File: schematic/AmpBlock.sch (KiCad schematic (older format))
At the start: 12 parts, among them IC8 LTC6090CS8E#PBF

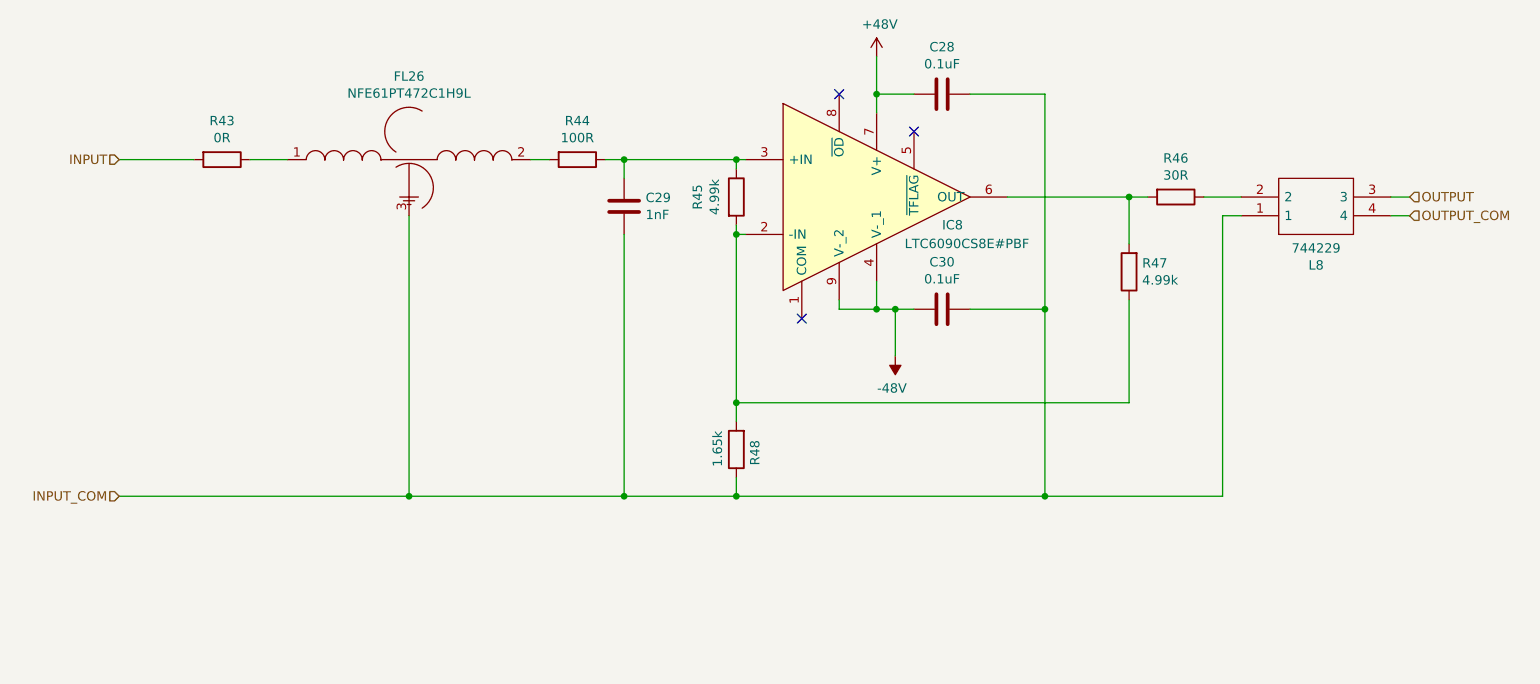
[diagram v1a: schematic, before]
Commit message: Board updates and starting to add more capacitors
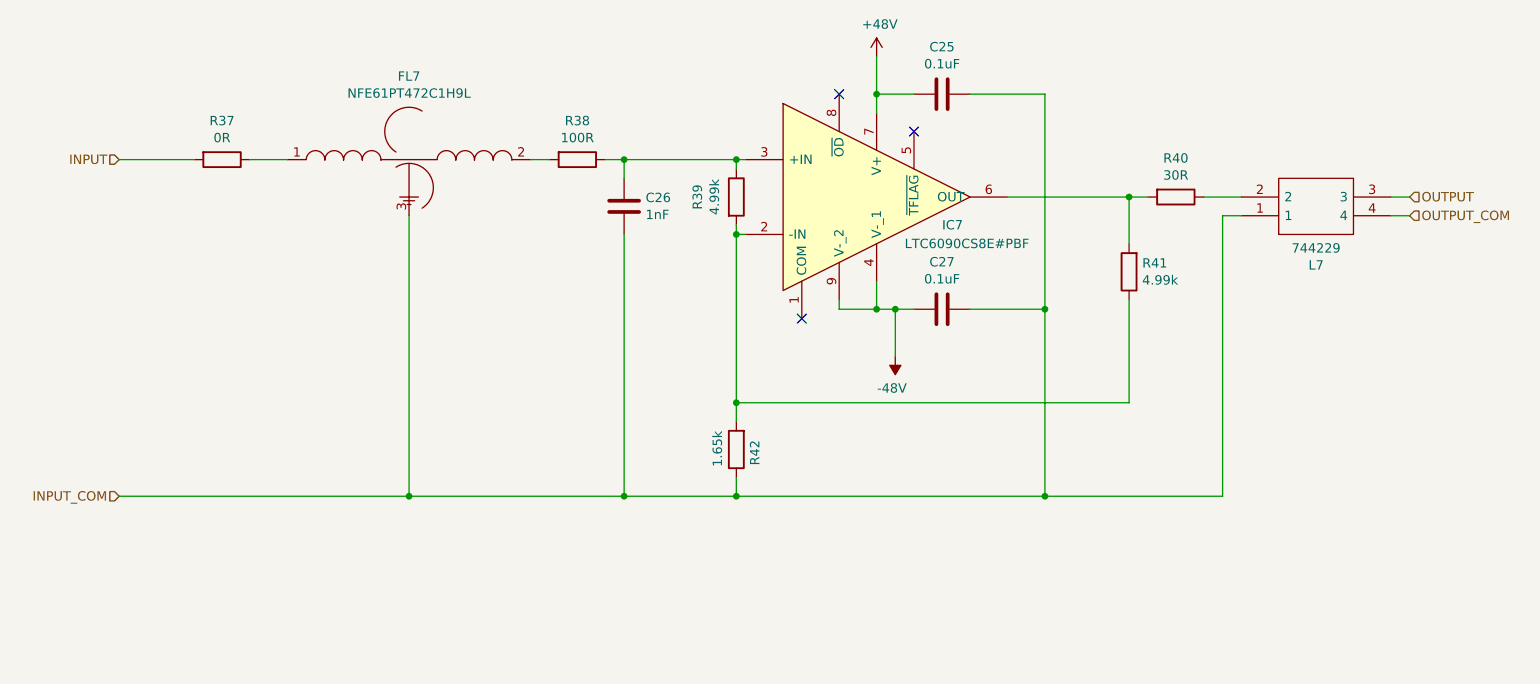
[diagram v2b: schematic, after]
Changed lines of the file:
@@
 $Descr A4 11693 8268
 encoding utf-8
-Sheet 26 33
+Sheet 8 33
 Title "Amplifier block"
 Date ""
@@
 AR Path="/5CAE2EB0/5C968DBB" Ref="R188"  Part="1"
 AR Path="/5C968DBB" Ref="R?"  Part="1"
-F 0 "R?" V 3743 3400 50  0000 C CNN
+F 0 "R38" V 3743 3400 50  0000 C CNN
 F 1 "100R" V 3834 3400 50  0000 C CNN
 F 2 "Resistor_SMD:R_0603_1608Metric" V 3880 3400 50  0001 C CNN
@@
 AR Path="/5CAE2EB0/5C969C02" Ref="R192"  Part="1"
 AR Path="/5C969C02" Ref="R?"  Part="1"
-F 0 "R?" V 4700 4900 50  0000 L CNN
+F 0 "R42" V 4700 4900 50  0000 L CNN
 F 1 "1.65k" V 4900 4850 50  0000 L CNN
 F 2 "Resistor_SMD:R_0603_1608Metric" V 4730 4950 50  0001 C CNN
@@
 AR Path="/5CAE2EB0/5C96A29C" Ref="R191"  Part="1"
 AR Path="/5C96A29C" Ref="R?"  Part="1"
-F 0 "R?" H 6830 3954 50  0000 R CNN
+F 0 "R41" H 6830 3954 50  0000 R CNN
 F 1 "4.99k" H 6830 4045 50  0000 R CNN
 F 2 "Resistor_SMD:R_0603_1608Metric" V 6830 4000 50  0001 C CNN
@@
 AR Path="/5CAE2EB0/5C96A628" Ref="C101"  Part="1"
 AR Path="/5C96A628" Ref="C?"  Part="1"
-F 0 "C?" H 4315 3696 50  0000 L CNN
+F 0 "C26" H 4315 3696 50  0000 L CNN
 F 1 "1nF" H 4315 3605 50  0000 L CNN
 F 2 "Capacitor_SMD:C_0603_1608Metric" H 4238 3500 50  0001 C CNN
@@
 AR Path="/5CAE2EB0/5C96EFD0" Ref="#PWR073"  Part="1"
 AR Path="/5C96EFD0" Ref="#PWR?"  Part="1"
-F 0 "#PWR063" H 5550 2700 50  0001 C CNN
+F 0 "#PWR023" H 5550 2700 50  0001 C CNN
 F 1 "+48V" H 5567 3023 50  0000 C CNN
 F 2 "" H 5550 2850 50  0001 C CNN
@@
 AR Path="/5CAE2EB0/5C96F7F1" Ref="#PWR074"  Part="1"
 AR Path="/5C96F7F1" Ref="#PWR?"  Part="1"
-F 0 "#PWR064" H 5650 4300 50  0001 C CNN
+F 0 "#PWR024" H 5650 4300 50  0001 C CNN
 F 1 "-48V" H 5668 4623 50  0000 C CNN
 F 2 "" H 5650 4450 50  0001 C CNN
@@
 AR Path="/5CAE2EB0/5C96FD85" Ref="C100"  Part="1"
 AR Path="/5C96FD85" Ref="C?"  Part="1"
-F 0 "C?" V 5648 3050 50  0000 C CNN
+F 0 "C25" V 5648 3050 50  0000 C CNN
 F 1 "0.1uF" V 5739 3050 50  0000 C CNN
 F 2 "Capacitor_SMD:C_0603_1608Metric" H 5938 2900 50  0001 C CNN
@@
 AR Path="/5CAE2EB0/5C97026D" Ref="C102"  Part="1"
 AR Path="/5C97026D" Ref="C?"  Part="1"
-F 0 "C?" V 5648 4200 50  0000 C CNN
+F 0 "C27" V 5648 4200 50  0000 C CNN
 F 1 "0.1uF" V 5739 4200 50  0000 C CNN
 F 2 "Capacitor_SMD:C_0603_1608Metric" H 5938 4050 50  0001 C CNN
@@
 AR Path="/5CAE2E6A/5E7F6ABF" Ref="FL31"  Part="1"
 AR Path="/5CAE2EB0/5E7F6ABF" Ref="FL32"  Part="1"
-F 0 "FL?" H 3050 3845 50  0000 C CNN
+F 0 "FL7" H 3050 3845 50  0000 C CNN
 F 1 "NFE61PT472C1H9L" H 3050 3754 50  0000 C CNN
 F 2 "ARTIQAmp:NFE61" H 3400 3650 50  0001 L CNN
@@
 AR Path="/5CAE2EB0/5F650121" Ref="R187"  Part="1"
 AR Path="/5F650121" Ref="R?"  Part="1"
-F 0 "R?" V 1843 3400 50  0000 C CNN
+F 0 "R37" V 1843 3400 50  0000 C CNN
 F 1 "0R" V 1934 3400 50  0000 C CNN
 F 2 "Resistor_SMD:R_0603_1608Metric" V 1980 3400 50  0001 C CNN
@@
 AR Path="/5CAE2EB0/5F6588CE" Ref="R189"  Part="1"
 AR Path="/5F6588CE" Ref="R?"  Part="1"
-F 0 "R?" V 4593 3600 50  0000 C CNN
+F 0 "R39" V 4593 3600 50  0000 C CNN
 F 1 "4.99k" V 4684 3600 50  0000 C CNN
 F 2 "Resistor_SMD:R_0603_1608Metric" V 4730 3600 50  0001 C CNN
@@
 AR Path="/5CAE2EB0/5F678EAA" Ref="R190"  Part="1"
 AR Path="/5F678EAA" Ref="R?"  Part="1"
-F 0 "R?" V 6943 3600 50  0000 C CNN
+F 0 "R40" V 6943 3600 50  0000 C CNN
 F 1 "30R" V 7034 3600 50  0000 C CNN
 F 2 "Resistor_SMD:R_0603_1608Metric" V 7080 3600 50  0001 C CNN
@@
 AR Path="/5CAE2E6A/5F68D18B" Ref="L31"  Part="1"
 AR Path="/5CAE2EB0/5F68D18B" Ref="L32"  Part="1"
-F 0 "L?" H 7900 3965 50  0000 C CNN
+F 0 "L7" H 7900 3965 50  0000 C CNN
 F 1 "744229" H 7900 3874 50  0000 C CNN
 F 2 "ARTIQAmp:WE-SL2" H 8150 3800 50  0001 L CNN
@@
 AR Path="/5CAE2E6A/5F68D7CC" Ref="IC31"  Part="1"
 AR Path="/5CAE2EB0/5F68D7CC" Ref="IC32"  Part="1"
-F 0 "IC?" H 5900 3450 50  0000 L CNN
+F 0 "IC7" H 5900 3450 50  0000 L CNN
 F 1 "LTC6090CS8E#PBF" H 5700 3350 50  0000 L CNN
 F 2 "ARTIQAmp:SOIC127P599X175-9N" H 5600 4200 50  0001 L CNN

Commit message: Many updates to layout; nearing final design
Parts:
- added R207, R208: 0R, Resistor_SMD:R_0603_1608Metric, symbol Device:R
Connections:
- net INPUT_COM: now also R207.2, R208.2
- new net GND: R207.1, R208.1
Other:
- note added: "Optional connections to ground plane"

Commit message: Penultimate tweaks
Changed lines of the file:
@@
 AR Path="/5CAE2EB0/5FE9E532" Ref="R188"  Part="1"
 AR Path="/5FE9E532" Ref="R?"  Part="1"
-F 0 "R38" V 3743 3400 50  0000 C CNN
+F 0 "R158" V 3743 3400 50  0000 C CNN
 F 1 "100R" V 3834 3400 50  0000 C CNN
 F 2 "Resistor_SMD:R_0603_1608Metric" V 3880 3400 50  0001 C CNN
@@
 AR Path="/5CAE2EB0/5C969C02" Ref="R192"  Part="1"
 AR Path="/5C969C02" Ref="R?"  Part="1"
-F 0 "R42" V 4700 4900 50  0000 L CNN
+F 0 "R162" V 4700 4900 50  0000 L CNN
 F 1 "1.65k" V 4900 4850 50  0000 L CNN
 F 2 "Resistor_SMD:R_0603_1608Metric" V 4730 4950 50  0001 C CNN
@@
 AR Path="/5CAE2EB0/5C96A29C" Ref="R191"  Part="1"
 AR Path="/5C96A29C" Ref="R?"  Part="1"
-F 0 "R41" H 6830 3954 50  0000 R CNN
+F 0 "R161" H 6830 3954 50  0000 R CNN
 F 1 "4.99k" H 6830 4045 50  0000 R CNN
 F 2 "Resistor_SMD:R_0603_1608Metric" V 6830 4000 50  0001 C CNN
@@
 AR Path="/5CAE2EB0/5C96A628" Ref="C101"  Part="1"
 AR Path="/5C96A628" Ref="C?"  Part="1"
-F 0 "C26" H 4315 3696 50  0000 L CNN
+F 0 "C86" H 4315 3696 50  0000 L CNN
 F 1 "1nF" H 4315 3605 50  0000 L CNN
 F 2 "Capacitor_SMD:C_0603_1608Metric" H 4238 3500 50  0001 C CNN
@@
 AR Path="/5CAE2EB0/5C96EFD0" Ref="#PWR073"  Part="1"
 AR Path="/5C96EFD0" Ref="#PWR?"  Part="1"
-F 0 "#PWR023" H 5550 2700 50  0001 C CNN
+F 0 "#PWR063" H 5550 2700 50  0001 C CNN
 F 1 "+48V" H 5567 3023 50  0000 C CNN
 F 2 "" H 5550 2850 50  0001 C CNN
@@
 AR Path="/5CAE2EB0/5FE9E537" Ref="#PWR074"  Part="1"
 AR Path="/5FE9E537" Ref="#PWR?"  Part="1"
-F 0 "#PWR024" H 5650 4300 50  0001 C CNN
+F 0 "#PWR064" H 5650 4300 50  0001 C CNN
 F 1 "-48V" H 5668 4623 50  0000 C CNN
 F 2 "" H 5650 4450 50  0001 C CNN
@@
 AR Path="/5CAE2EB0/5C96FD85" Ref="C100"  Part="1"
 AR Path="/5C96FD85" Ref="C?"  Part="1"
-F 0 "C25" V 5648 3050 50  0000 C CNN
+F 0 "C85" V 5648 3050 50  0000 C CNN
 F 1 "0.1uF" V 5739 3050 50  0000 C CNN
 F 2 "Capacitor_SMD:C_0603_1608Metric" H 5938 2900 50  0001 C CNN
@@
 AR Path="/5CAE2EB0/5FE9E539" Ref="C102"  Part="1"
 AR Path="/5FE9E539" Ref="C?"  Part="1"
-F 0 "C27" V 5648 4200 50  0000 C CNN
+F 0 "C87" V 5648 4200 50  0000 C CNN
 F 1 "0.1uF" V 5739 4200 50  0000 C CNN
 F 2 "Capacitor_SMD:C_0603_1608Metric" H 5938 4050 50  0001 C CNN
@@
 AR Path="/5CAE2E6A/5E7F6ABF" Ref="FL31"  Part="1"
 AR Path="/5CAE2EB0/5E7F6ABF" Ref="FL32"  Part="1"
-F 0 "FL7" H 3050 3845 50  0000 C CNN
+F 0 "FL27" H 3050 3845 50  0000 C CNN
 F 1 "NFE61PT472C1H9L" H 3050 3754 50  0000 C CNN
 F 2 "ARTIQAmp:NFE61" H 3400 3650 50  0001 L CNN
@@
 AR Path="/5CAE2EB0/5F650121" Ref="R187"  Part="1"
 AR Path="/5F650121" Ref="R?"  Part="1"
-F 0 "R37" V 1843 3400 50  0000 C CNN
+F 0 "R157" V 1843 3400 50  0000 C CNN
 F 1 "0R" V 1934 3400 50  0000 C CNN
 F 2 "Resistor_SMD:R_0603_1608Metric" V 1980 3400 50  0001 C CNN
@@
 AR Path="/5CAE2EB0/5F6588CE" Ref="R189"  Part="1"
 AR Path="/5F6588CE" Ref="R?"  Part="1"
-F 0 "R39" V 4593 3600 50  0000 C CNN
+F 0 "R159" V 4593 3600 50  0000 C CNN
 F 1 "4.99k" V 4684 3600 50  0000 C CNN
 F 2 "Resistor_SMD:R_0603_1608Metric" V 4730 3600 50  0001 C CNN
@@
 AR Path="/5CAE2EB0/5F678EAA" Ref="R190"  Part="1"
 AR Path="/5F678EAA" Ref="R?"  Part="1"
-F 0 "R40" V 6943 3600 50  0000 C CNN
+F 0 "R160" V 6943 3600 50  0000 C CNN
 F 1 "30R" V 7034 3600 50  0000 C CNN
 F 2 "Resistor_SMD:R_0603_1608Metric" V 7080 3600 50  0001 C CNN
@@
 AR Path="/5CAE2E6A/5F68D18B" Ref="L31"  Part="1"
 AR Path="/5CAE2EB0/5F68D18B" Ref="L32"  Part="1"
-F 0 "L7" H 7900 3965 50  0000 C CNN
+F 0 "L27" H 7900 3965 50  0000 C CNN
 F 1 "744229" H 7900 3874 50  0000 C CNN
 F 2 "ARTIQAmp:WE-SL2" H 8150 3800 50  0001 L CNN
@@
 AR Path="/5CAE2E6A/5F68D7CC" Ref="IC31"  Part="1"
 AR Path="/5CAE2EB0/5F68D7CC" Ref="IC32"  Part="1"
-F 0 "IC7" H 5900 3450 50  0000 L CNN
+F 0 "IC27" H 5900 3450 50  0000 L CNN
 F 1 "LTC6090CS8E#PBF" H 5700 3350 50  0000 L CNN
 F 2 "ARTIQAmp:SOIC127P599X175-9N" H 5600 4200 50  0001 L CNN
@@
 AR Path="/5CAE2EB0/5F8DFD1E" Ref="#PWR0135"  Part="1"
 AR Path="/5CAE2E52/5F8DFD1E" Ref="#PWR0136"  Part="1"
-F 0 "#PWR0111" H 3050 5650 50  0001 C CNN
+F 0 "#PWR0136" H 3050 5650 50  0001 C CNN
 F 1 "GND" H 3055 5727 50  0000 C CNN
 F 2 "" H 3050 5900 50  0001 C CNN
@@
 AR Path="/5CAE2EB0/5F8E08A0" Ref="R253"  Part="1"
 AR Path="/5F8E08A0" Ref="R?"  Part="1"
-F 0 "R205" V 2800 5500 50  0000 L CNN
+F 0 "R255" V 2800 5500 50  0000 L CNN
 F 1 "0R" V 3000 5450 50  0000 L CNN
 F 2 "Resistor_SMD:R_0603_1608Metric" V 2830 5550 50  0001 C CNN
@@
 AR Path="/5CAE2EB0/5F8E1BE6" Ref="R254"  Part="1"
 AR Path="/5F8E1BE6" Ref="R?"  Part="1"
-F 0 "R206" V 3100 5500 50  0000 L CNN
+F 0 "R256" V 3100 5500 50  0000 L CNN
 F 1 "0R" V 3300 5450 50  0000 L CNN
 F 2 "Resistor_SMD:R_0603_1608Metric" V 3130 5550 50  0001 C CNN

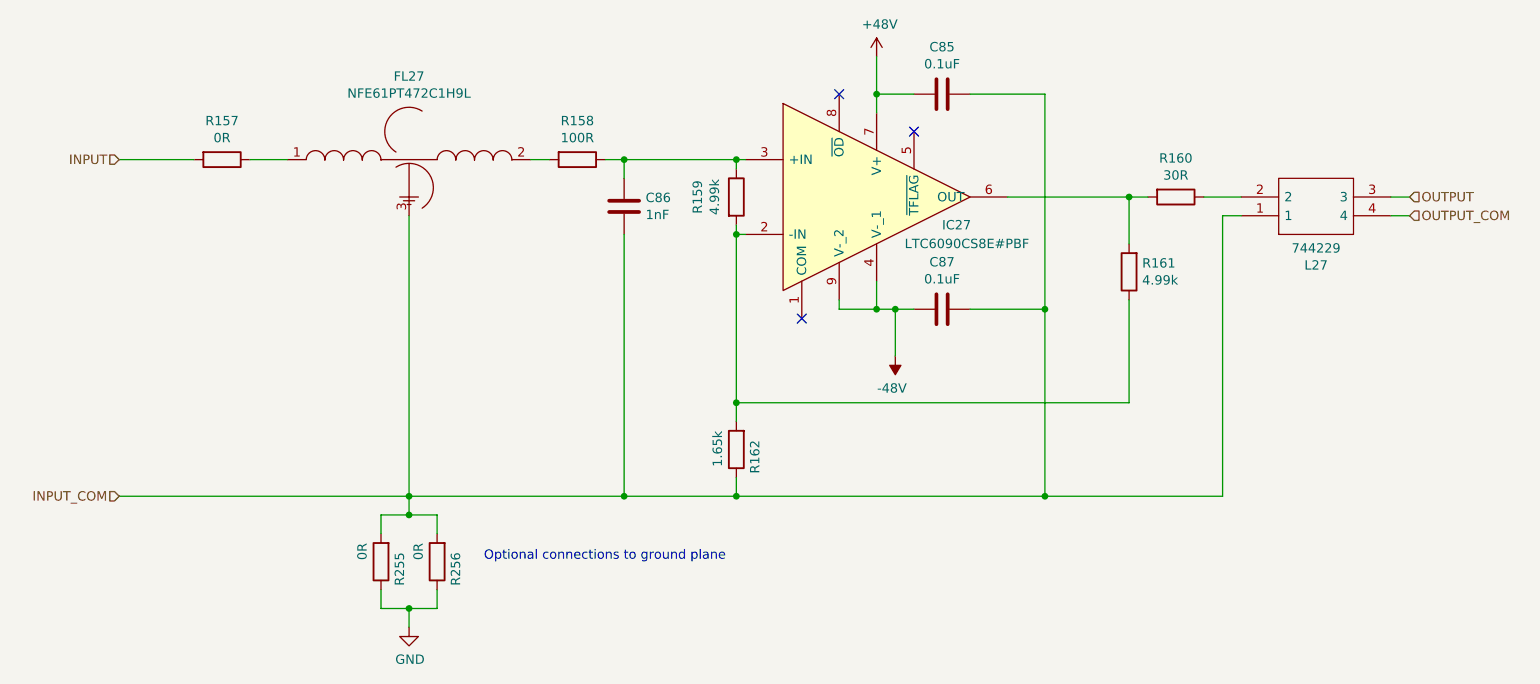
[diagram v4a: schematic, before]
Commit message: Saftey commit before adding new shorting resistors
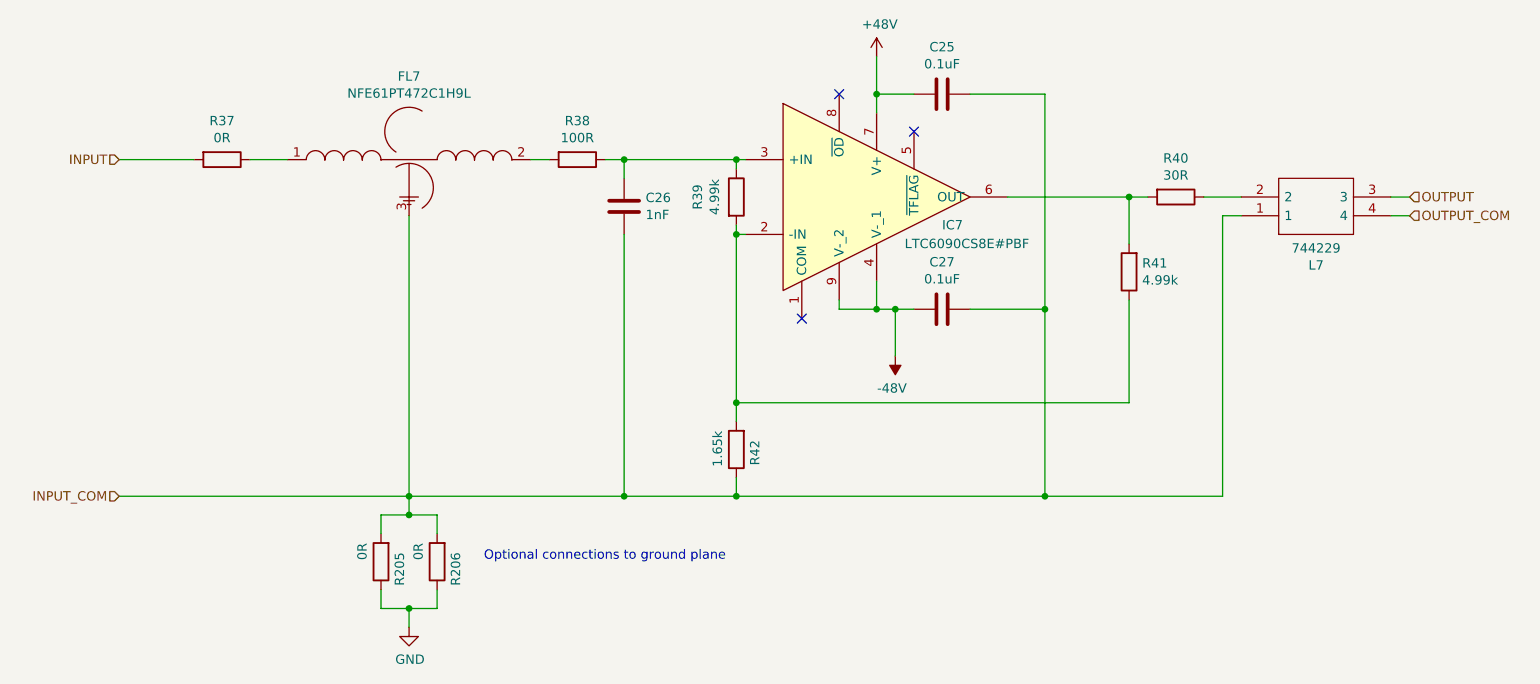
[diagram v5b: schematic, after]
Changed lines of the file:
@@
 AR Path="/5CAE2EB0/5FE9E532" Ref="R188"  Part="1"
 AR Path="/5FE9E532" Ref="R?"  Part="1"
-F 0 "R158" V 3743 3400 50  0000 C CNN
+F 0 "R38" V 3743 3400 50  0000 C CNN
 F 1 "100R" V 3834 3400 50  0000 C CNN
 F 2 "Resistor_SMD:R_0603_1608Metric" V 3880 3400 50  0001 C CNN
@@
 AR Path="/5CAE2EB0/5C969C02" Ref="R192"  Part="1"
 AR Path="/5C969C02" Ref="R?"  Part="1"
-F 0 "R162" V 4700 4900 50  0000 L CNN
+F 0 "R42" V 4700 4900 50  0000 L CNN
 F 1 "1.65k" V 4900 4850 50  0000 L CNN
 F 2 "Resistor_SMD:R_0603_1608Metric" V 4730 4950 50  0001 C CNN
@@
 AR Path="/5CAE2EB0/5C96A29C" Ref="R191"  Part="1"
 AR Path="/5C96A29C" Ref="R?"  Part="1"
-F 0 "R161" H 6830 3954 50  0000 R CNN
+F 0 "R41" H 6830 3954 50  0000 R CNN
 F 1 "4.99k" H 6830 4045 50  0000 R CNN
 F 2 "Resistor_SMD:R_0603_1608Metric" V 6830 4000 50  0001 C CNN
@@
 AR Path="/5CAE2EB0/5C96A628" Ref="C101"  Part="1"
 AR Path="/5C96A628" Ref="C?"  Part="1"
-F 0 "C86" H 4315 3696 50  0000 L CNN
+F 0 "C26" H 4315 3696 50  0000 L CNN
 F 1 "1nF" H 4315 3605 50  0000 L CNN
 F 2 "Capacitor_SMD:C_0603_1608Metric" H 4238 3500 50  0001 C CNN
@@
 AR Path="/5CAE2EB0/5C96EFD0" Ref="#PWR073"  Part="1"
 AR Path="/5C96EFD0" Ref="#PWR?"  Part="1"
-F 0 "#PWR063" H 5550 2700 50  0001 C CNN
+F 0 "#PWR023" H 5550 2700 50  0001 C CNN
 F 1 "+48V" H 5567 3023 50  0000 C CNN
 F 2 "" H 5550 2850 50  0001 C CNN
@@
 AR Path="/5CAE2EB0/5FE9E537" Ref="#PWR074"  Part="1"
 AR Path="/5FE9E537" Ref="#PWR?"  Part="1"
-F 0 "#PWR064" H 5650 4300 50  0001 C CNN
+F 0 "#PWR024" H 5650 4300 50  0001 C CNN
 F 1 "-48V" H 5668 4623 50  0000 C CNN
 F 2 "" H 5650 4450 50  0001 C CNN
@@
 AR Path="/5CAE2EB0/5C96FD85" Ref="C100"  Part="1"
 AR Path="/5C96FD85" Ref="C?"  Part="1"
-F 0 "C85" V 5648 3050 50  0000 C CNN
+F 0 "C25" V 5648 3050 50  0000 C CNN
 F 1 "0.1uF" V 5739 3050 50  0000 C CNN
 F 2 "Capacitor_SMD:C_0603_1608Metric" H 5938 2900 50  0001 C CNN
@@
 AR Path="/5CAE2EB0/5FE9E539" Ref="C102"  Part="1"
 AR Path="/5FE9E539" Ref="C?"  Part="1"
-F 0 "C87" V 5648 4200 50  0000 C CNN
+F 0 "C27" V 5648 4200 50  0000 C CNN
 F 1 "0.1uF" V 5739 4200 50  0000 C CNN
 F 2 "Capacitor_SMD:C_0603_1608Metric" H 5938 4050 50  0001 C CNN
@@
 AR Path="/5CAE2E6A/5E7F6ABF" Ref="FL31"  Part="1"
 AR Path="/5CAE2EB0/5E7F6ABF" Ref="FL32"  Part="1"
-F 0 "FL27" H 3050 3845 50  0000 C CNN
+F 0 "FL7" H 3050 3845 50  0000 C CNN
 F 1 "NFE61PT472C1H9L" H 3050 3754 50  0000 C CNN
 F 2 "ARTIQAmp:NFE61" H 3400 3650 50  0001 L CNN
@@
 AR Path="/5CAE2EB0/5F650121" Ref="R187"  Part="1"
 AR Path="/5F650121" Ref="R?"  Part="1"
-F 0 "R157" V 1843 3400 50  0000 C CNN
+F 0 "R37" V 1843 3400 50  0000 C CNN
 F 1 "0R" V 1934 3400 50  0000 C CNN
 F 2 "Resistor_SMD:R_0603_1608Metric" V 1980 3400 50  0001 C CNN
@@
 AR Path="/5CAE2EB0/5F6588CE" Ref="R189"  Part="1"
 AR Path="/5F6588CE" Ref="R?"  Part="1"
-F 0 "R159" V 4593 3600 50  0000 C CNN
+F 0 "R39" V 4593 3600 50  0000 C CNN
 F 1 "4.99k" V 4684 3600 50  0000 C CNN
 F 2 "Resistor_SMD:R_0603_1608Metric" V 4730 3600 50  0001 C CNN
@@
 AR Path="/5CAE2EB0/5F678EAA" Ref="R190"  Part="1"
 AR Path="/5F678EAA" Ref="R?"  Part="1"
-F 0 "R160" V 6943 3600 50  0000 C CNN
+F 0 "R40" V 6943 3600 50  0000 C CNN
 F 1 "30R" V 7034 3600 50  0000 C CNN
 F 2 "Resistor_SMD:R_0603_1608Metric" V 7080 3600 50  0001 C CNN
@@
 AR Path="/5CAE2E6A/5F68D18B" Ref="L31"  Part="1"
 AR Path="/5CAE2EB0/5F68D18B" Ref="L32"  Part="1"
-F 0 "L27" H 7900 3965 50  0000 C CNN
+F 0 "L7" H 7900 3965 50  0000 C CNN
 F 1 "744229" H 7900 3874 50  0000 C CNN
 F 2 "ARTIQAmp:WE-SL2" H 8150 3800 50  0001 L CNN
@@
 AR Path="/5CAE2E6A/5F68D7CC" Ref="IC31"  Part="1"
 AR Path="/5CAE2EB0/5F68D7CC" Ref="IC32"  Part="1"
-F 0 "IC27" H 5900 3450 50  0000 L CNN
+F 0 "IC7" H 5900 3450 50  0000 L CNN
 F 1 "LTC6090CS8E#PBF" H 5700 3350 50  0000 L CNN
 F 2 "ARTIQAmp:SOIC127P599X175-9N" H 5600 4200 50  0001 L CNN
@@
 AR Path="/5CAE2EB0/5F8DFD1E" Ref="#PWR0135"  Part="1"
 AR Path="/5CAE2E52/5F8DFD1E" Ref="#PWR0136"  Part="1"
-F 0 "#PWR0136" H 3050 5650 50  0001 C CNN
+F 0 "#PWR0111" H 3050 5650 50  0001 C CNN
 F 1 "GND" H 3055 5727 50  0000 C CNN
 F 2 "" H 3050 5900 50  0001 C CNN
@@
 AR Path="/5CAE2EB0/5F8E08A0" Ref="R253"  Part="1"
 AR Path="/5F8E08A0" Ref="R?"  Part="1"
-F 0 "R255" V 2800 5500 50  0000 L CNN
+F 0 "R205" V 2800 5500 50  0000 L CNN
 F 1 "0R" V 3000 5450 50  0000 L CNN
 F 2 "Resistor_SMD:R_0603_1608Metric" V 2830 5550 50  0001 C CNN
@@
 AR Path="/5CAE2EB0/5F8E1BE6" Ref="R254"  Part="1"
 AR Path="/5F8E1BE6" Ref="R?"  Part="1"
-F 0 "R256" V 3100 5500 50  0000 L CNN
+F 0 "R206" V 3100 5500 50  0000 L CNN
 F 1 "0R" V 3300 5450 50  0000 L CNN
 F 2 "Resistor_SMD:R_0603_1608Metric" V 3130 5550 50  0001 C CNN
